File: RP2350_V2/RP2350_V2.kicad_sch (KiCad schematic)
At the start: 106 parts, among them IC1 DMP1045U-7, IC2 DMP1045U-7, IC3 DMP1045U-7, IC4 DMP1045U-7, J1 Conn_01x04_Pin, J3 USB_C_Receptacle_USB2.0_16P, J5 Conn_01x08_Socket, J6 Conn_01x02_Pin, J7 Conn_01x04_Pin, SW1 PTS 647 SN50 SMTR2 LFS, SW10 PTS 647 SN50 SMTR2 LFS, SW11 PTS 647 SN50 SMTR2 LFS, SW12 PTS 647 SN50 SMTR2 LFS, SW13 PTS 647 SN50 SMTR2 LFS, SW14 PTS 647 SN50 SMTR2 LFS, SW4 PTS 647 SN50 SMTR2 LFS, SW9 PTS 647 SN50 SMTR2 LFS, U1 RP2350_60QFN, U2 W25Q128JVS, U3 TPS62811QWRWYRQ1, U4 MCP73812T-420I-OT, U5 TLV3012AIDCKR, U6 74HC14, X1 ABM8-272-T3

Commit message: Transceiver components and schematic final?
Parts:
- L1: footprint My_Global_Inductors:AOTA-B201610S3R3-101-T -> My_Footprints:AOTA-B201610S3R3-101-T

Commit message: progress :D
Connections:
- net GND: now also J6.2 (Pin_2); no longer J6.1 (Pin_1)
- net SPI0_CLK: no longer U1.37 (GPIO25)
- net SPI0_RX: no longer U1.35 (GPIO23)
- net VBAT: now also J6.1 (Pin_1); no longer J6.2 (Pin_2)
- new net SPIO_CLK: U1.37 (GPIO25)
- new net SPIO_RX: U1.35 (GPIO23)
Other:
- moved on the sheet: J6
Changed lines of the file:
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@@
 	)
 	(junction
-		(at 162.56 240.03)
-		(diameter 0)
-		(color 0 0 0 0)
-	)
-	(junction
 		(at 114.3 83.82)
 		(diameter 0)
@@
 	)
 	(junction
+		(at 163.83 240.03)
+		(diameter 0)
+		(color 0 0 0 0)
+	)
+	(junction
 		(at 187.96 223.52)
 		(diameter 0)
@@
 	(wire
 		(pts
-			(xy 148.59 240.03) (xy 162.56 240.03)
+			(xy 148.59 240.03) (xy 163.83 240.03)
 		)
 		(stroke
@@
 	(wire
 		(pts
+			(xy 163.83 251.46) (xy 163.83 254)
+		)
+		(stroke
+			(width 0)
+			(type default)
+		)
+	)
+	(wire
+		(pts
 			(xy 304.8 62.23) (xy 309.88 62.23)
 		)
@@
 	(wire
 		(pts
-			(xy 162.56 248.92) (xy 162.56 254)
-		)
-		(stroke
-			(width 0)
-			(type default)
-		)
-	)
-	(wire
-		(pts
 			(xy 391.16 234.95) (xy 391.16 238.76)
 		)
@@
 	(wire
 		(pts
+			(xy 163.83 240.03) (xy 165.1 240.03)
+		)
+		(stroke
+			(width 0)
+			(type default)
+		)
+	)
+	(wire
+		(pts
 			(xy 269.24 80.01) (xy 269.24 81.28)
 		)
@@
 	(wire
 		(pts
-			(xy 162.56 240.03) (xy 162.56 246.38)
+			(xy 163.83 240.03) (xy 163.83 248.92)
 		)
 		(stroke
@@
 	(wire
 		(pts
-			(xy 148.59 254) (xy 162.56 254)
+			(xy 148.59 254) (xy 163.83 254)
 		)
 		(stroke
@@
 		)
 	)
-	(wire
-		(pts
-			(xy 162.56 240.03) (xy 165.1 240.03)
-		)
-		(stroke
-			(width 0)
-			(type default)
-		)
-	)
 	(polyline
 		(pts
@@
 		)
 	)
-	(label "CS{slash}NSS"
-		(at 373.38 149.86 0)
-		(effects
-			(font
-				(size 1.27 1.27)
-			)
-			(justify left bottom)
-		)
-	)
 	(label "QSPI_SCLK"
 		(at 215.9 191.77 0)
@@
 		)
 	)
-	(label "SPI0_RX"
-		(at 373.38 147.32 0)
-		(effects
-			(font
-				(size 1.27 1.27)
-			)
-			(justify left bottom)
-		)
-	)
-	(label "SPI0_CLK"
-		(at 373.38 152.4 0)
-		(effects
-			(font
-				(size 1.27 1.27)
-			)
-			(justify left bottom)
-		)
-	)
 	(label "QSPI_SD3"
 		(at 288.29 111.76 0)
@@
 		)
 	)
-	(label "SPI0_TX"
-		(at 373.38 137.16 0)
-		(effects
-			(font
-				(size 1.27 1.27)
-			)
-			(justify left bottom)
-		)
-	)
 	(label "VBUS_5V"
 		(at 52.07 223.52 0)
@@
 		)
 	)
-	(label "DIO1"
-		(at 373.38 144.78 0)
-		(effects
-			(font
-				(size 1.27 1.27)
-			)
-			(justify left bottom)
-		)
-	)
 	(label "XOUT"
 		(at 294.64 129.54 0)
@@
 		)
 	)
-	(label "uC_RESET"
-		(at 373.38 139.7 0)
-		(effects
-			(font
-				(size 1.27 1.27)
-			)
-			(justify left bottom)
-		)
-	)
 	(label "SPI0_RX"
 		(at 199.39 76.2 0)
@@
 		)
 	)
-	(label "uC_BUSY"
-		(at 373.38 142.24 0)
-		(effects
-			(font
-				(size 1.27 1.27)
-			)
-			(justify left bottom)
-		)
-	)
 	(label "DISPLAY_RESET"
 		(at 373.38 111.76 0)
@@
 		)
 	)
+	(global_label "SPIO_CLK"
+		(shape input)
+		(at 373.38 152.4 0)
+		(fields_autoplaced yes)
+		(effects
+			(font
+				(size 1.27 1.27)
+			)
+			(justify left)
+		)
+		(property "Intersheetrefs" "${INTERSHEET_REFS}"
+			(at 385.3157 152.4 0)
+			(effects
+				(font
+					(size 1.27 1.27)
+				)
+				(justify left)
+				(hide yes)
+			)
+		)
+	)
+	(global_label "CS{slash}NSS"
+		(shape input)
+		(at 373.38 149.86 0)
+		(fields_autoplaced yes)
+		(effects
+			(font
+				(size 1.27 1.27)
+			)
+			(justify left)
+		)
+		(property "Intersheetrefs" "${INTERSHEET_REFS}"
+			(at 383.9247 149.86 0)
+			(effects
+				(font
+					(size 1.27 1.27)
+				)
+				(justify left)
+				(hide yes)
+			)
+		)
+	)
+	(global_label "uC_BUSY"
+		(shape input)
+		(at 373.38 142.24 0)
+		(fields_autoplaced yes)
+		(effects
+			(font
+				(size 1.27 1.27)
+			)
+			(justify left)
+		)
+		(property "Intersheetrefs" "${INTERSHEET_REFS}"
+			(at 384.6504 142.24 0)
+			(effects
+				(font
+					(size 1.27 1.27)
+				)
+				(justify left)
+				(hide yes)
+			)
+		)
+	)
+	(global_label "uC_RESET"
+		(shape input)
+		(at 373.38 139.7 0)
+		(fields_autoplaced yes)
+		(effects
+			(font
+				(size 1.27 1.27)
+			)
+			(justify left)
+		)
+		(property "Intersheetrefs" "${INTERSHEET_REFS}"
+			(at 385.4969 139.7 0)
+			(effects
+				(font
+					(size 1.27 1.27)
+				)
+				(justify left)
+				(hide yes)
+			)
+		)
+	)
+	(global_label "SPIO_RX"
+		(shape input)
+		(at 373.38 147.32 0)
+		(fields_autoplaced yes)
+		(effects
+			(font
+				(size 1.27 1.27)
+			)
+			(justify left)
+		)
+		(property "Intersheetrefs" "${INTERSHEET_REFS}"
+			(at 384.2271 147.32 0)
+			(effects
+				(font
+					(size 1.27 1.27)
+				)
+				(justify left)
+				(hide yes)
+			)
+		)
+	)
+	(global_label "SPI0_TX"
+		(shape input)
+		(at 373.38 137.16 0)
+		(fields_autoplaced yes)
+		(effects
+			(font
+				(size 1.27 1.27)
+			)
+			(justify left)
+		)
+		(property "Intersheetrefs" "${INTERSHEET_REFS}"
+			(at 383.8037 137.16 0)
+			(effects
+				(font
+					(size 1.27 1.27)
+				)
+				(justify left)
+				(hide yes)
+			)
+		)
+	)
+	(global_label "DIO1"
+		(shape input)
+		(at 373.38 144.78 0)
+		(fields_autoplaced yes)
+		(effects
+			(font
+				(size 1.27 1.27)
+			)
+			(justify left)
+		)
+		(property "Intersheetrefs" "${INTERSHEET_REFS}"
+			(at 380.78 144.78 0)
+			(effects
+				(font
+					(size 1.27 1.27)
+				)
+				(justify left)
+				(hide yes)
+			)
+		)
+	)
 	(symbol
 		(lib_id "Mechanical:MountingHole")
@@
 	(symbol
 		(lib_id "Connector:Conn_01x02_Pin")
-		(at 167.64 248.92 180)
+		(at 168.91 248.92 0)
+		(mirror y)
 		(unit 1)
 		(exclude_from_sim no)
@@
 		(dnp no)
 		(property "Reference" "J6"
-			(at 164.592 252.984 0)
+			(at 165.862 244.856 0)
 			(effects
 				(font
@@
 		)
 		(property "Value" "Conn_01x02_Pin"
-			(at 171.45 250.698 0)
+			(at 172.72 247.142 0)
 			(effects
 				(font
@@
 		)
 		(property "Footprint" "Connector_JST:JST_PH_B2B-PH-K_1x02_P2.00mm_Vertical"
-			(at 167.64 248.92 0)
+			(at 168.91 248.92 0)
 			(effects
 				(font
@@
 		)
 		(property "Datasheet" "~"
-			(at 167.64 248.92 0)
+			(at 168.91 248.92 0)
 			(effects
 				(font
@@
 		)
 		(property "Description" "Generic connector, single row, 01x02, script generated"
-			(at 167.64 248.92 0)
+			(at 168.91 248.92 0)
 			(effects
 				(font
@@
 		)
 		(property "LCSC" "C131337"
-			(at 167.64 248.92 0)
+			(at 168.91 248.92 0)
 			(effects
 				(font
@@
 		)
 		(property "SNAPEDA_PN" ""
-			(at 167.64 248.92 0)
+			(at 168.91 248.92 0)
 			(effects
 				(font

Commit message: rev2 progress
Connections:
- net CS/NSS: now also U1.13 (GPIO9); no longer U1.36 (GPIO24)
- net DIO1: now also U1.18 (GPIO14); no longer U1.34 (GPIO22)
- net DISPLAY_BUSY: now also J5.3 (Pin_3), U1.31 (GPIO19); no longer J5.8 (Pin_8), U1.12 (GPIO8)
- net DISPLAY_DC: now also J5.5 (Pin_5), U1.33 (GPIO21); no longer J5.6 (Pin_6), U1.14 (GPIO10)
- net DISPLAY_RESET: now also J5.4 (Pin_4), U1.32 (GPIO20); no longer J5.7 (Pin_7), U1.13 (GPIO9)
- net SPI0_TX: now also U1.15 (GPIO11); no longer U1.31 (GPIO19)
- net SPI1_CLK: now also J5.7 (Pin_7), U1.35 (GPIO23); no longer J5.4 (Pin_4), U1.16 (GPIO12)
- net SPI1_CS: now also J5.6 (Pin_6), U1.34 (GPIO22); no longer J5.5 (Pin_5), U1.15 (GPIO11)
- net SPI1_TX: now also J5.8 (Pin_8), U1.36 (GPIO24); no longer J5.3 (Pin_3), U1.17 (GPIO13)
- net SPIO_CLK: now also U1.14 (GPIO10); no longer U1.37 (GPIO25)
- net SPIO_RX: now also U1.12 (GPIO8); no longer U1.35 (GPIO23)
- net VBUS: now also U4.1 (CE)
- net uC_BUSY: now also U1.17 (GPIO13); no longer U1.33 (GPIO21)
- net uC_RESET: now also U1.16 (GPIO12); no longer U1.32 (GPIO20)
- no-connect marks 12 -> 11
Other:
- moved on the sheet: C17

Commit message: Lots of Updatesgit add --allgit add --all
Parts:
- added IC5, IC6: DMP1045U-7, My_Footprints:SOT96P240X110-3N, symbol My_Library:DMP1045U-7
- added J10, J2, J8, J9: S0991-46R, My_Footprints:HARWIN_S0991-46R, symbol My_Library:S0991-46R
- added R39: 100k, Resistor_SMD:R_0402_1005Metric, symbol Device:R
- R28: value 86.6 -> 110; LCSC C270575 -> C25078
- R32: value 75 -> 91; LCSC C25133 -> C270397
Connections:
- net +3V3: now also J5.8 (Pin_8); no longer J5.1 (Pin_1)
- net DIO1: now also U1.28 (GPIO17); no longer U1.18 (GPIO14)
- net DISPLAY_BUSY: now also J5.1 (Pin_1); no longer J5.3 (Pin_3)
- net DISPLAY_DC: now also J5.3 (Pin_3); no longer J5.5 (Pin_5)
- net DISPLAY_RESET: now also J5.2 (Pin_2); no longer J5.4 (Pin_4)
- net GND: now also J5.7 (Pin_7), IC5.3 (D), IC6.3 (D), J10.SH1 (SHIELD), J10.SH2 (SHIELD__1), J10.SH3 (SHIELD__2), J2.SH1 (SHIELD), J2.SH2 (SHIELD__1), J2.SH3 (SHIELD__2), J8.SH1 (SHIELD), J8.SH2 (SHIELD__1), J8.SH3 (SHIELD__2), J9.SH1 (SHIELD), J9.SH2 (SHIELD__1), J9.SH3 (SHIELD__2); no longer D5.C, J5.2 (Pin_2)
- net RUN: now also R31.1; no longer R31.2
- net SPI1_CLK: now also J5.5 (Pin_5); no longer J5.7 (Pin_7)
- net SPI1_CS: now also J5.4 (Pin_4); no longer J5.6 (Pin_6)
- net SPI1_TX: now also J5.6 (Pin_6); no longer J5.8 (Pin_8)
- net SPIO_RX: now also U1.16 (GPIO12); no longer U1.12 (GPIO8)
- net UVLO_RST: now also IC5.1 (G); no longer R31.1
- net VBUS: now also R39.1
- net uC_BUSY: now also U1.27 (GPIO16); no longer U1.17 (GPIO13)
- net uC_RESET: now also U1.17 (GPIO13); no longer U1.16 (GPIO12)
- new net: IC5.2 (S), R31.2
- new net: IC6.1 (G), R39.2
- new net: D5.C, IC6.2 (S)
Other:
- note added: "RST"
- moved on the sheet: C21, C22, C23, C24, C25, C26, C27, D4, J1, J5, J7, R16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

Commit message: optimizations, refinements
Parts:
- J10, J2, J8, J9: LCSC (none) -> C3308732
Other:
- note added: "RF Shield"
- note added: "Transceiver"
- moved on the sheet: D4, J10, J2, J8, J9, R28, R37, R39

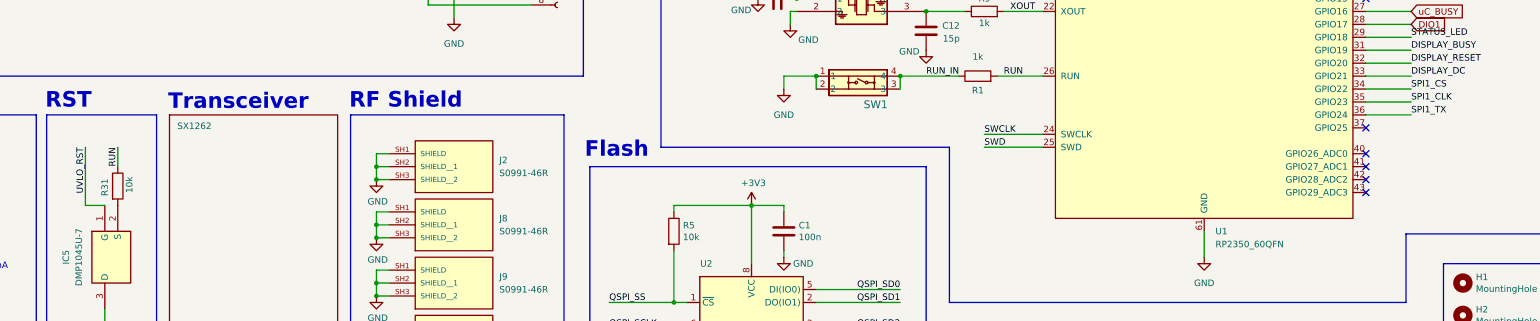
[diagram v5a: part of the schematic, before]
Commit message: added 3V3 input to ADC, fixed edge cut DRCs
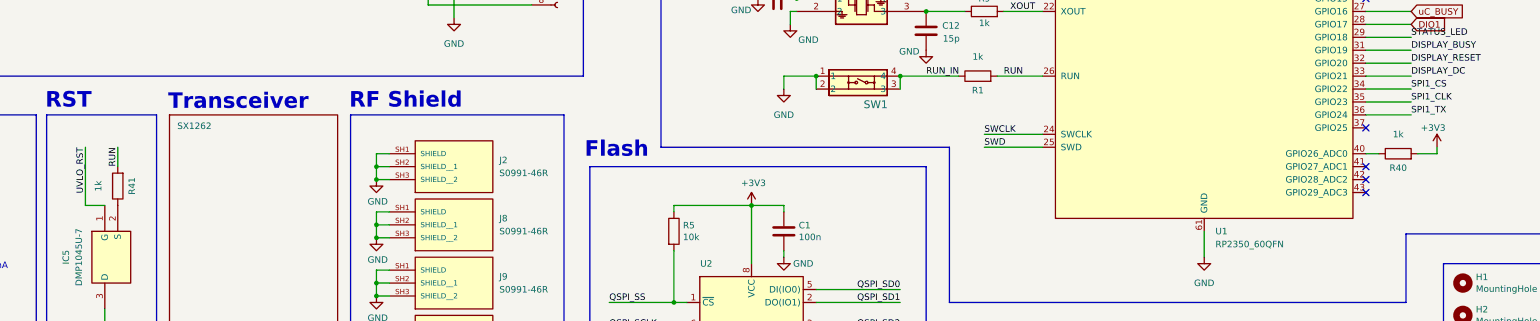
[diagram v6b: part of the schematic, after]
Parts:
- removed R31: 10k, Resistor_SMD:R_0402_1005Metric, symbol Device:R
- added R40, R41: 1k, Resistor_SMD:R_0402_1005Metric, symbol Device:R
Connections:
- net +3V3: now also R40.2
- net RUN: now also R41.2
- net at IC5.2 (S): now also R41.1
- net at U1.40 (GPIO26_ADC0): now also R40.1
- no-connect marks 11 -> 10
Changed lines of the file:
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@@
 	)
 	(no_connect
-		(at 364.49 157.48)
-	)
-	(no_connect
 		(at 50.8 254)
 	)
@@
 	(wire
 		(pts
+			(xy 378.46 156.21) (xy 378.46 157.48)
+		)
+		(stroke
+			(width 0)
+			(type default)
+		)
+	)
+	(wire
+		(pts
 			(xy 102.87 44.45) (xy 102.87 46.99)
 		)
@@
 	(wire
 		(pts
+			(xy 378.46 157.48) (xy 374.65 157.48)
+		)
+		(stroke
+			(width 0)
+			(type default)
+		)
+	)
+	(wire
+		(pts
 			(xy 187.96 81.28) (xy 200.66 81.28)
 		)
@@
 	(wire
 		(pts
+			(xy 364.49 157.48) (xy 367.03 157.48)
+		)
+		(stroke
+			(width 0)
+			(type default)
+		)
+	)
+	(wire
+		(pts
 			(xy 288.29 109.22) (xy 300.99 109.22)
 		)
@@
 	)
 	(symbol
-		(lib_id "Device:R")
-		(at 119.38 163.83 0)
-		(unit 1)
-		(exclude_from_sim no)
-		(in_bom yes)
-		(on_board yes)
-		(dnp no)
-		(property "Reference" "R31"
-			(at 116.84 164.084 90)
-			(effects
-				(font
-					(size 1.27 1.27)
-				)
-			)
-		)
-		(property "Value" "10k"
-			(at 121.666 163.576 90)
-			(effects
-				(font
-					(size 1.27 1.27)
-				)
-			)
-		)
-		(property "Footprint" "Resistor_SMD:R_0402_1005Metric"
-			(at 117.602 163.83 90)
-			(effects
-				(font
-					(size 1.27 1.27)
-				)
-				(hide yes)
-			)
-		)
-		(property "Datasheet" "~"
-			(at 119.38 163.83 0)
-			(effects
-				(font
-					(size 1.27 1.27)
-				)
-				(hide yes)
-			)
-		)
-		(property "Description" "Resistor"
-			(at 119.38 163.83 0)
-			(effects
-				(font
-					(size 1.27 1.27)
-				)
-				(hide yes)
-			)
-		)
-		(property "LCSC" "C25744"
-			(at 119.38 163.83 90)
-			(effects
-				(font
-					(size 1.27 1.27)
-				)
-				(hide yes)
-			)
-		)
-		(property "SNAPEDA_PN" ""
-			(at 119.38 163.83 0)
-			(effects
-				(font
-					(size 1.27 1.27)
-				)
-				(hide yes)
-			)
-		)
-		(pin "1"
-		)
-		(pin "2"
-		)
-		(instances
-			(project "RP2350_V2"
-				(path "/7f0ba00e-9b42-4d85-a00a-8f4530ab07c8"
-					(reference "R31")
-					(unit 1)
-				)
-			)
-		)
-	)
-	(symbol
 		(lib_id "Device:C")
 		(at 133.35 111.76 0)
@@
 	(symbol
 		(lib_id "Device:R")
+		(at 370.84 157.48 90)
+		(unit 1)
+		(exclude_from_sim no)
+		(in_bom yes)
+		(on_board yes)
+		(dnp no)
+		(property "Reference" "R40"
+			(at 370.84 160.274 90)
+			(effects
+				(font
+					(size 1.27 1.27)
+				)
+			)
+		)
+		(property "Value" "1k"
+			(at 370.84 153.67 90)
+			(effects
+				(font
+					(size 1.27 1.27)
+				)
+			)
+		)
+		(property "Footprint" "Resistor_SMD:R_0402_1005Metric"
+			(at 370.84 159.258 90)
+			(effects
+				(font
+					(size 1.27 1.27)
+				)
+				(hide yes)
+			)
+		)
+		(property "Datasheet" "~"
+			(at 370.84 157.48 0)
+			(effects
+				(font
+					(size 1.27 1.27)
+				)
+				(hide yes)
+			)
+		)
+		(property "Description" "Resistor"
+			(at 370.84 157.48 0)
+			(effects
+				(font
+					(size 1.27 1.27)
+				)
+				(hide yes)
+			)
+		)
+		(property "LCSC" "C11702"
+			(at 370.84 157.48 90)
+			(effects
+				(font
+					(size 1.27 1.27)
+				)
+				(hide yes)
+			)
+		)
+		(property "SNAPEDA_PN" ""
+			(at 370.84 157.48 0)
+			(effects
+				(font
+					(size 1.27 1.27)
+				)
+				(hide yes)
+			)
+		)
+		(pin "1"
+		)
+		(pin "2"
+		)
+		(instances
+			(project "RP2350_V2"
+				(path "/7f0ba00e-9b42-4d85-a00a-8f4530ab07c8"
+					(reference "R40")
+					(unit 1)
+				)
+			)
+		)
+	)
+	(symbol
+		(lib_id "Device:R")
 		(at 82.55 166.37 0)
 		(mirror y)
@@
 	(symbol
 		(lib_id "Device:R")
+		(at 119.38 163.83 180)
+		(unit 1)
+		(exclude_from_sim no)
+		(in_bom yes)
+		(on_board yes)
+		(dnp no)
+		(property "Reference" "R41"
+			(at 122.174 163.83 90)
+			(effects
+				(font
+					(size 1.27 1.27)
+				)
+			)
+		)
+		(property "Value" "1k"
+			(at 115.57 163.83 90)
+			(effects
+				(font
+					(size 1.27 1.27)
+				)
+			)
+		)
+		(property "Footprint" "Resistor_SMD:R_0402_1005Metric"
+			(at 121.158 163.83 90)
+			(effects
+				(font
+					(size 1.27 1.27)
+				)
+				(hide yes)
+			)
+		)
+		(property "Datasheet" "~"
+			(at 119.38 163.83 0)
+			(effects
+				(font
+					(size 1.27 1.27)
+				)
+				(hide yes)
+			)
+		)
+		(property "Description" "Resistor"
+			(at 119.38 163.83 0)
+			(effects
+				(font
+					(size 1.27 1.27)
+				)
+				(hide yes)
+			)
+		)
+		(property "LCSC" "C11702"
+			(at 119.38 163.83 90)
+			(effects
+				(font
+					(size 1.27 1.27)
+				)
+				(hide yes)
+			)
+		)
+		(property "SNAPEDA_PN" ""
+			(at 119.38 163.83 0)
+			(effects
+				(font
+					(size 1.27 1.27)
+				)
+				(hide yes)
+			)
+		)
+		(pin "1"
+		)
+		(pin "2"
+		)
+		(instances
+			(project "RP2350_V2"
+				(path "/7f0ba00e-9b42-4d85-a00a-8f4530ab07c8"
+					(reference "R41")
+					(unit 1)
+				)
+			)
+		)
+	)
+	(symbol
+		(lib_id "Device:R")
 		(at 74.93 238.76 0)
 		(unit 1)
@@
 					(unit 1)
 				)
+			)
+		)
+	)
+	(symbol
+		(lib_id "power:+3V3")
+		(at 378.46 156.21 0)
+		(unit 1)
+		(exclude_from_sim no)
+		(in_bom yes)
+		(on_board yes)
+		(dnp no)
+		(property "Reference" "#PWR094"
+			(at 378.46 160.02 0)
+			(effects
+				(font
+					(size 1.27 1.27)
+				)
+				(hide yes)
+			)
+		)
+		(property "Value" "+3V3"
+			(at 377.698 152.4 0)
+			(effects
+				(font
+					(size 1.27 1.27)
+				)
+			)
+		)
+		(property "Footprint" ""
+			(at 378.46 156.21 0)
+			(effects
+				(font
+					(size 1.27 1.27)
+				)
+				(hide yes)
+			)
+		)
+		(property "Datasheet" ""
+			(at 378.46 156.21 0)
+			(effects
+				(font
+					(size 1.27 1.27)
+				)
+				(hide yes)
+			)
+		)
+		(property "Description" ""
+			(at 378.46 156.21 0)
+			(effects
+				(font
+					(size 1.27 1.27)
+				)
+				(hide yes)
+			)
+		)
+		(pin "1"
+		)
+		(instances
+			(project "RP2350_V2"
+				(path "/7f0ba00e-9b42-4d85-a00a-8f4530ab07c8"
+					(reference "#PWR094")
+					(unit 1)
+				)

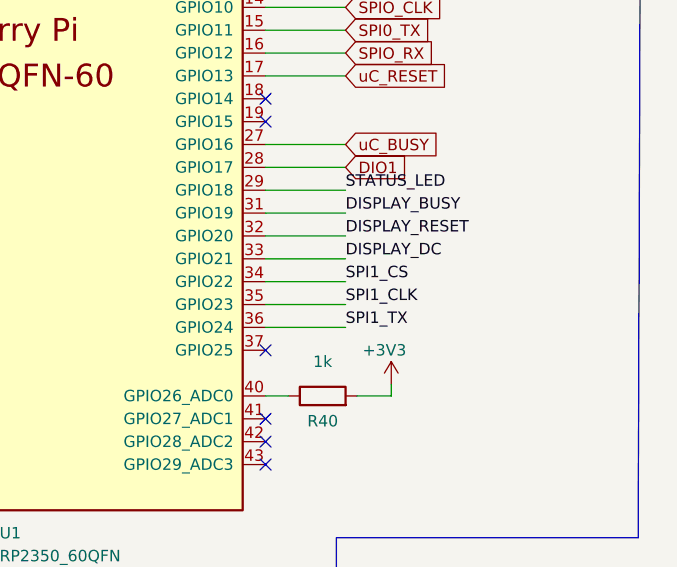
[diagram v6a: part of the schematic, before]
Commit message: fix display pins on mcu
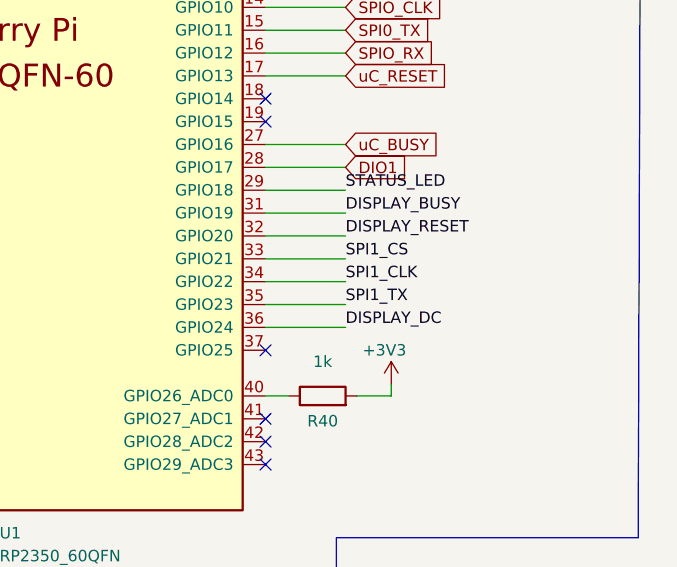
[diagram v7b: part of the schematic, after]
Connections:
- net DISPLAY_DC: now also U1.36 (GPIO24); no longer U1.33 (GPIO21)
- net SPI1_CLK: now also U1.34 (GPIO22); no longer U1.35 (GPIO23)
- net SPI1_CS: now also U1.33 (GPIO21); no longer U1.34 (GPIO22)
- net SPI1_TX: now also U1.35 (GPIO23); no longer U1.36 (GPIO24)

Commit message: dfdjfjh pt2
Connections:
- net SPIO_CLK is gone; now on net SPI0_CLK: U1.14 (GPIO10)
